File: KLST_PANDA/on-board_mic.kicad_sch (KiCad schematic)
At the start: 0 parts

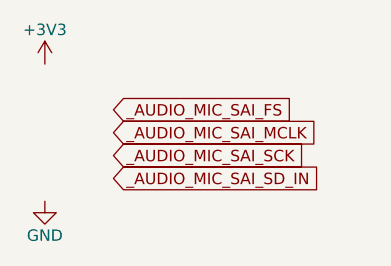
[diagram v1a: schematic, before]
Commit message: added PDM interface ( and removed SAI )
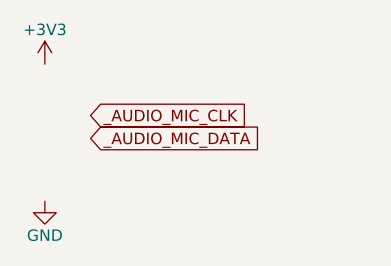
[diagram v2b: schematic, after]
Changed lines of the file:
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@@
 (kicad_sch (version 20230121) (generator eeschema)
   (paper "A4")
-  (global_label "_AUDIO_MIC_SAI_MCLK" (shape input) (at 142.875 101.6 0) (fields_autoplaced)
+  (global_label "_AUDIO_MIC_CLK" (shape input) (at 140.335 99.695 0) (fields_autoplaced)
     (effects (font (size 1.27 1.27)) (justify left))
-    (property "Intersheetrefs" "${INTERSHEET_REFS}" (at 166.5242 101.6 0)
+    (property "Intersheetrefs" "${INTERSHEET_REFS}" (at 158.6623 99.695 0)
       (effects (font (size 1.27 1.27)) (justify left) hide)
     )
   )
-  (global_label "_AUDIO_MIC_SAI_SD_IN" (shape input) (at 142.875 106.68 0) (fields_autoplaced)
+  (global_label "_AUDIO_MIC_DATA" (shape input) (at 140.335 102.235 0) (fields_autoplaced)
     (effects (font (size 1.27 1.27)) (justify left))
-    (property "Intersheetrefs" "${INTERSHEET_REFS}" (at 166.8871 106.68 0)
+    (property "Intersheetrefs" "${INTERSHEET_REFS}" (at 159.509 102.235 0)
       (effects (font (size 1.27 1.27)) (justify left) hide)
     )
-  )
-  (global_label "_AUDIO_MIC_SAI_FS" (shape input) (at 142.875 99.06 0) (fields_autoplaced)
-    (effects (font (size 1.27 1.27)) (justify left))
-    (property "Intersheetrefs" "${INTERSHEET_REFS}" (at 163.8028 99.06 0)
-      (effects (font (size 1.27 1.27)) (justify left) hide)
-    )
-  )
-  (global_label "_AUDIO_MIC_SAI_SCK" (shape input) (at 142.875 104.14 0) (fields_autoplaced)
-    (effects (font (size 1.27 1.27)) (justify left))
-    (property "Intersheetrefs" "${INTERSHEET_REFS}" (at 165.2542 104.14 0)
-      (effects (font (size 1.27 1.27)) (justify left) hide)
-    )

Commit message: added MEMS mics
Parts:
- added C72: 100nF, symbol Device:C_Small
- added C73: 1uF, symbol Device:C_Polarized_Small
- added U7, U8: MP34DT05TR-A, MP34DT05TR-A_STM, symbol MP34DT05TR-A:MP34DT05TR-A
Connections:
- net +3V3: now also C72.1, C73.1, U7.1 (VDD), U7.2 (LR), U8.1 (VDD)
- net GND: now also C72.2, C73.2, U7.5 (GND), U8.2 (LR), U8.5 (GND)
- net _AUDIO_MIC_CLK: now also U7.3 (CLK), U8.3 (CLK)
- net _AUDIO_MIC_DATA: now also U7.4 (DOUT), U8.4 (DOUT)
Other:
- note added: "on-board microphones"

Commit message: added mechanical keys, updated audio jacks, minor changes
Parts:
- U7, U8: footprint MP34DT05TR-A_STM -> MP34DT05TR-A:MP34DT05TR-A_STM
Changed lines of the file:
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@@
       (effects (font (size 1.524 1.524)))
     )
-    (property "Footprint" "MP34DT05TR-A_STM" (at 110.49 93.98 0)
+    (property "Footprint" "MP34DT05TR-A:MP34DT05TR-A_STM" (at 110.49 93.98 0)
       (effects (font (size 1.27 1.27) italic) hide)
     )
@@
       (effects (font (size 1.524 1.524)))
     )
-    (property "Footprint" "MP34DT05TR-A_STM" (at 110.49 118.745 0)
+    (property "Footprint" "MP34DT05TR-A:MP34DT05TR-A_STM" (at 110.49 118.745 0)
       (effects (font (size 1.27 1.27) italic) hide)
     )

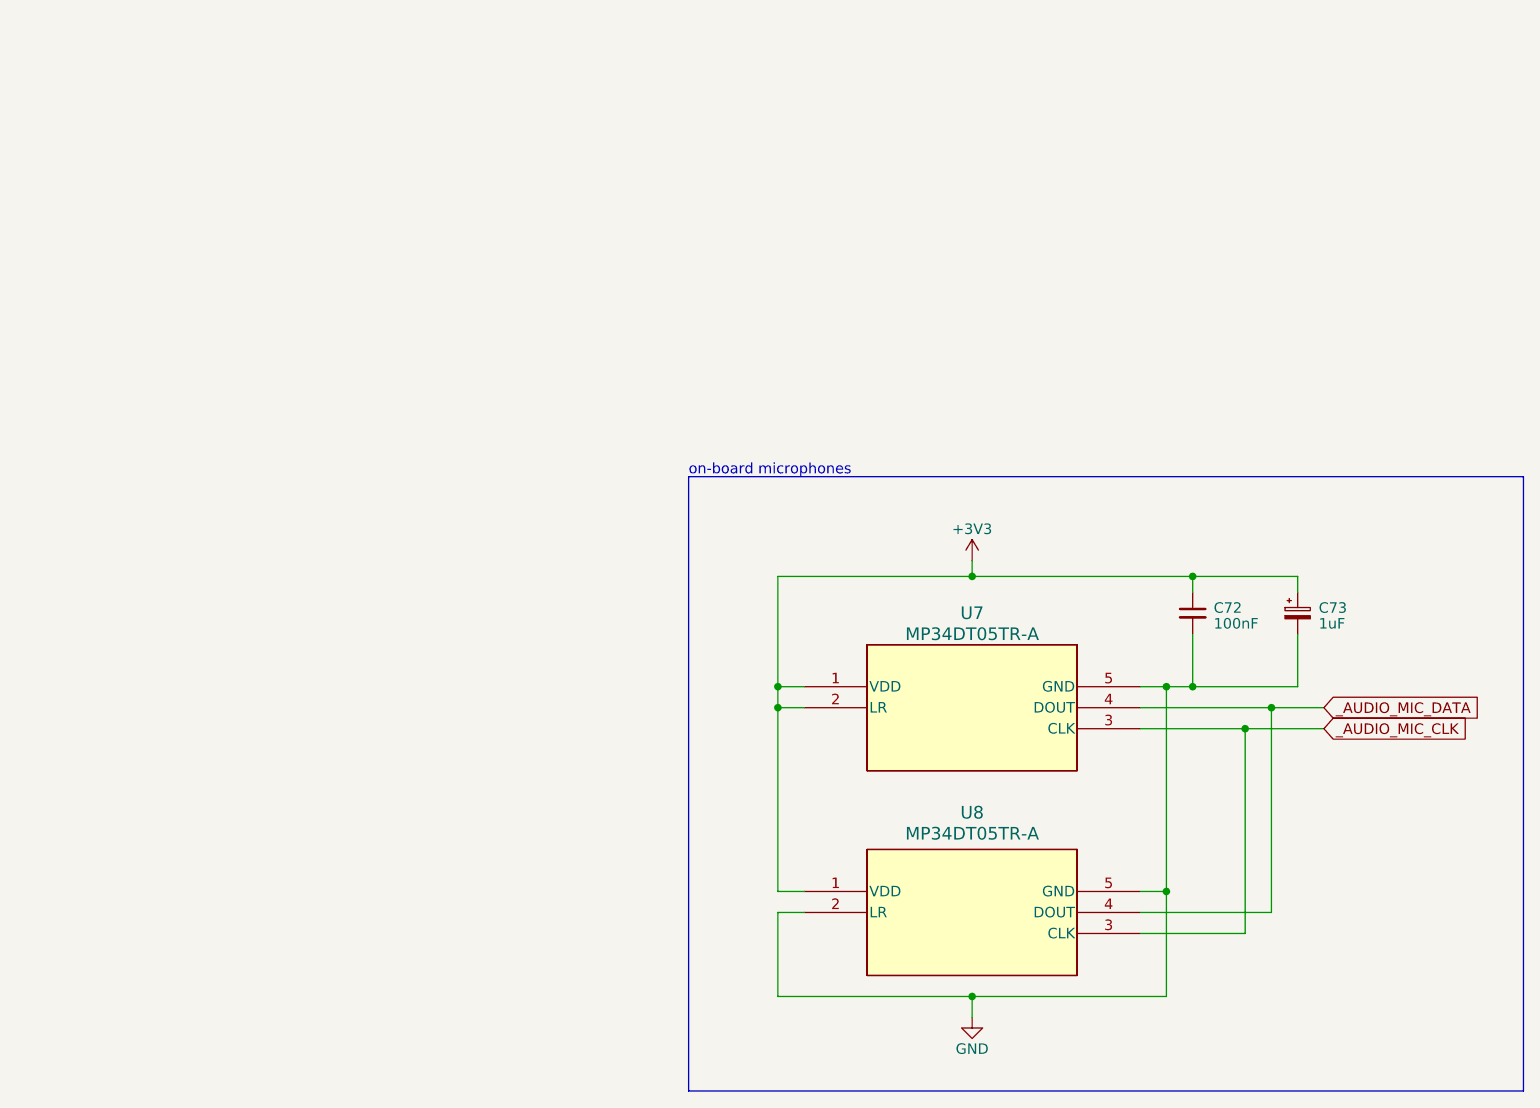
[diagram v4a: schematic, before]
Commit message: moved core (MCU) to sheet, cleaned up sheets
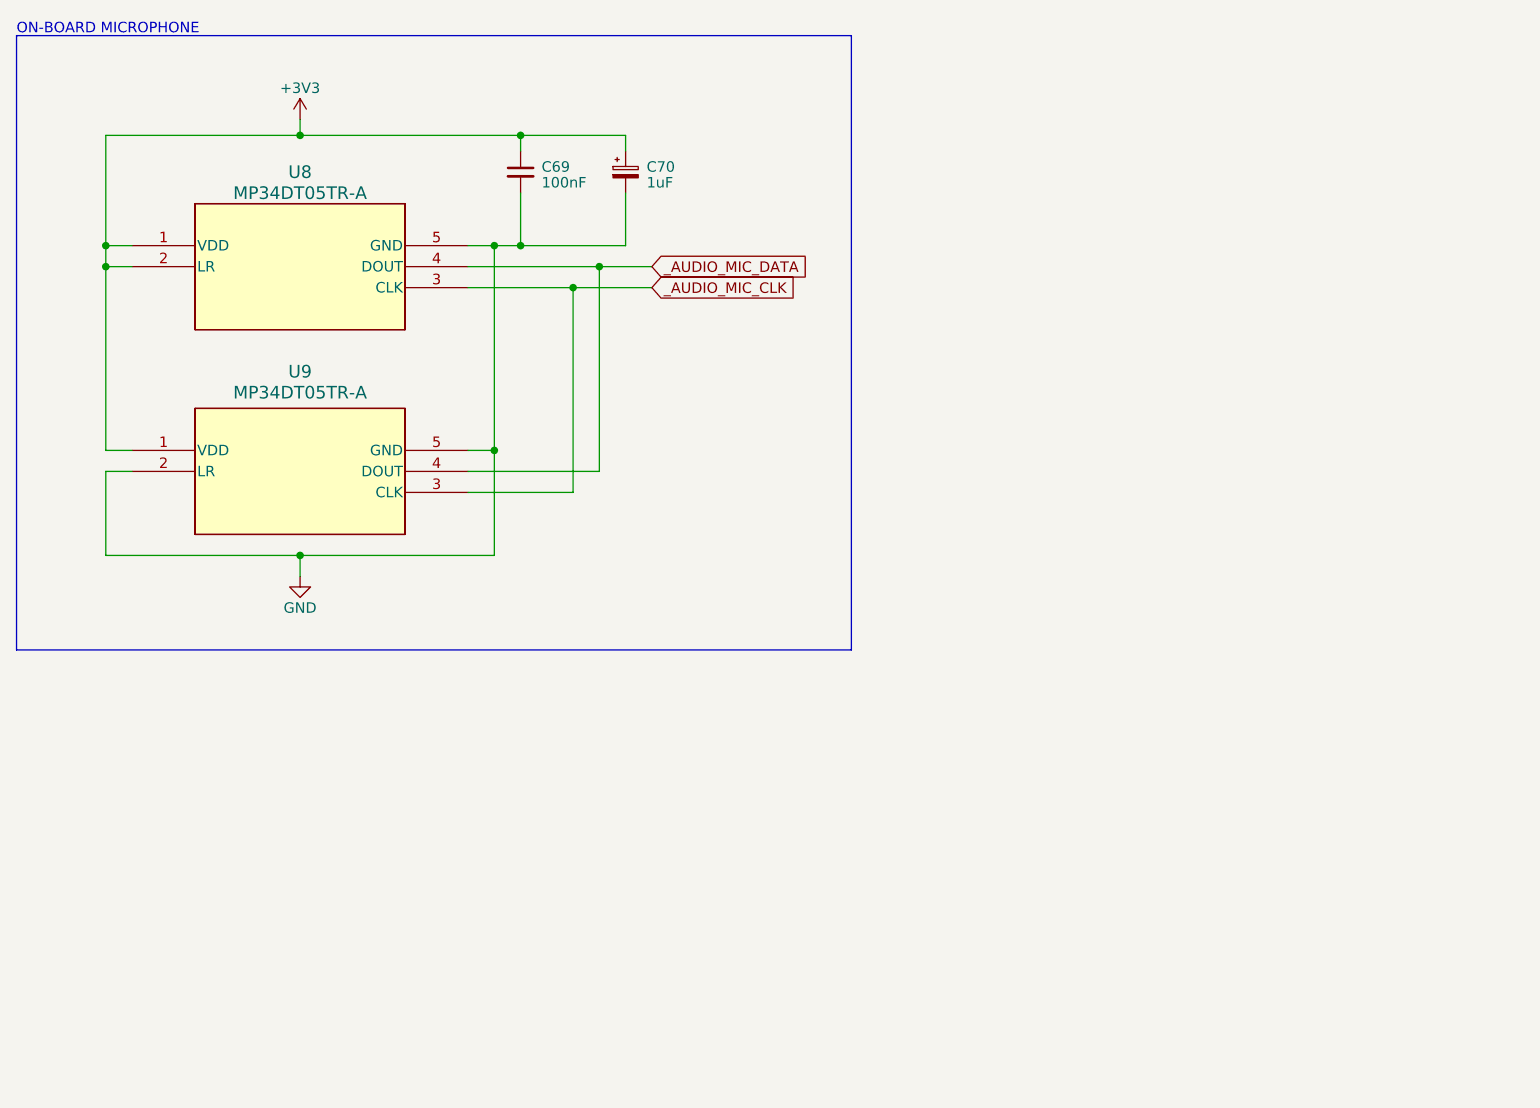
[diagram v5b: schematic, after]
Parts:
- renumbered C72 to C69, C73 to C70, U7 to U8, U8 to U9
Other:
- note added: "ON-BOARD MICROPHONE"
- note removed: "on-board microphones"
- moved on the sheet: C69, C70, U8, U9

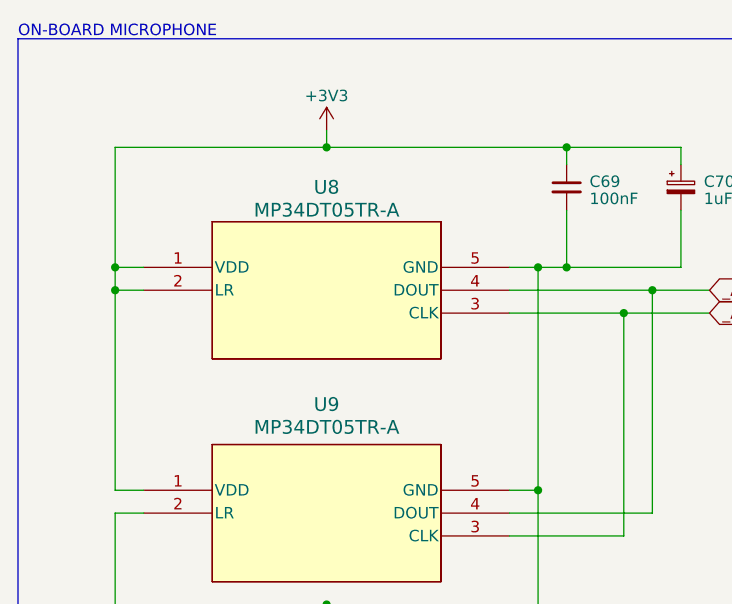
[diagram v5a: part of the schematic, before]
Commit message: started cleaning up schematic ( addressing DRC errors/warning ) (WIP)
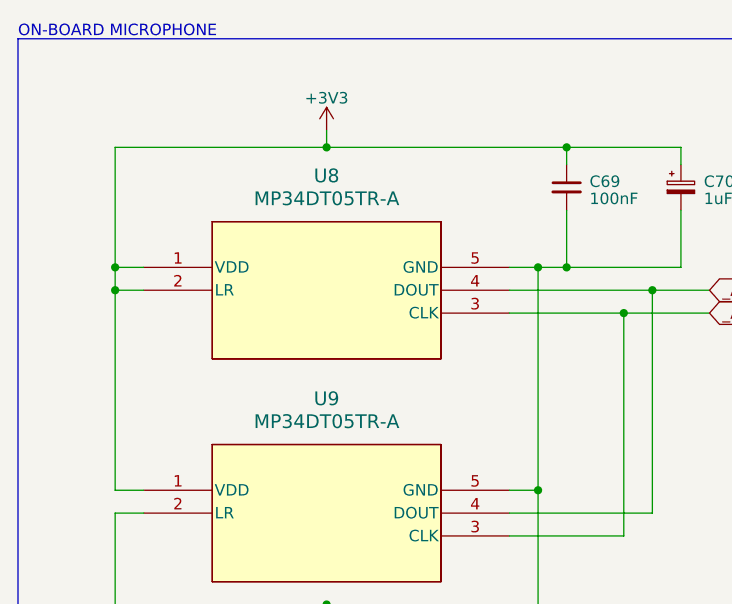
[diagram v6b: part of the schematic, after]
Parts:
- U8, U9: footprint MP34DT05TR-A:MP34DT05TR-A_STM -> MP34DT05TR-A_STM
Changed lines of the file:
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@@
       (effects (font (size 1.27 1.27)) hide)
     )
-    (property "Value" "+3V3" (at 49.53 21.59 0)
+    (property "Value" "+3V3" (at 49.53 21.844 0)
       (effects (font (size 1.27 1.27)))
     )
@@
         )
         (path "/b4513875-4c57-4720-bcc5-43ead67fe18f/47e8e77e-c64e-4c44-bfd8-2073580a3d85"
-          (reference "#PWR088") (unit 1)
+          (reference "#PWR089") (unit 1)
         )
       )
@@
   (symbol (lib_name "MP34DT05TR-A_1") (lib_id "MP34DT05TR-A:MP34DT05TR-A") (at 29.21 40.64 0) (unit 1)
     (in_bom yes) (on_board yes) (dnp no) (fields_autoplaced)
-    (property "Reference" "U8" (at 49.53 31.75 0)
+    (property "Reference" "U8" (at 49.53 30.48 0)
       (effects (font (size 1.524 1.524)))
     )
-    (property "Value" "MP34DT05TR-A" (at 49.53 34.29 0)
+    (property "Value" "MP34DT05TR-A" (at 49.53 33.02 0)
       (effects (font (size 1.524 1.524)))
     )
-    (property "Footprint" "MP34DT05TR-A:MP34DT05TR-A_STM" (at 29.21 40.64 0)
+    (property "Footprint" "MP34DT05TR-A_STM" (at 29.21 40.64 0)
       (effects (font (size 1.27 1.27) italic) hide)
     )
@@
     )
     (pin "1")
-    (pin "2")
     (pin "3")
     (pin "4")
+    (pin "2")
     (pin "5")
     (instances
@@
         )
         (path "/b4513875-4c57-4720-bcc5-43ead67fe18f/47e8e77e-c64e-4c44-bfd8-2073580a3d85"
-          (reference "#PWR089") (unit 1)
+          (reference "#PWR090") (unit 1)
         )
       )
@@
   (symbol (lib_id "MP34DT05TR-A:MP34DT05TR-A") (at 29.21 65.405 0) (unit 1)
     (in_bom yes) (on_board yes) (dnp no) (fields_autoplaced)
-    (property "Reference" "U9" (at 49.53 55.88 0)
+    (property "Reference" "U9" (at 49.53 55.245 0)
       (effects (font (size 1.524 1.524)))
     )
-    (property "Value" "MP34DT05TR-A" (at 49.53 58.42 0)
+    (property "Value" "MP34DT05TR-A" (at 49.53 57.785 0)
       (effects (font (size 1.524 1.524)))
     )
-    (property "Footprint" "MP34DT05TR-A:MP34DT05TR-A_STM" (at 29.21 65.405 0)
+    (property "Footprint" "MP34DT05TR-A_STM" (at 29.21 65.405 0)
       (effects (font (size 1.27 1.27) italic) hide)
     )
@@
     )
     (pin "1")
-    (pin "2")
     (pin "3")
     (pin "4")
+    (pin "2")
     (pin "5")
     (instances

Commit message: added battery clip, updated to new KiCad version
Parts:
- U8, U9: footprint MP34DT05TR-A_STM -> MP34DT05TR-A:MP34DT05TR-A_STM
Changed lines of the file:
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@@
       (effects (font (size 1.524 1.524)))
     )
-    (property "Footprint" "MP34DT05TR-A_STM" (at 29.21 40.64 0)
+    (property "Footprint" "MP34DT05TR-A:MP34DT05TR-A_STM" (at 29.21 40.64 0)
       (effects (font (size 1.27 1.27) italic) hide)
     )
@@
       (effects (font (size 1.524 1.524)))
     )
-    (property "Footprint" "MP34DT05TR-A_STM" (at 29.21 65.405 0)
+    (property "Footprint" "MP34DT05TR-A:MP34DT05TR-A_STM" (at 29.21 65.405 0)
       (effects (font (size 1.27 1.27) italic) hide)
     )

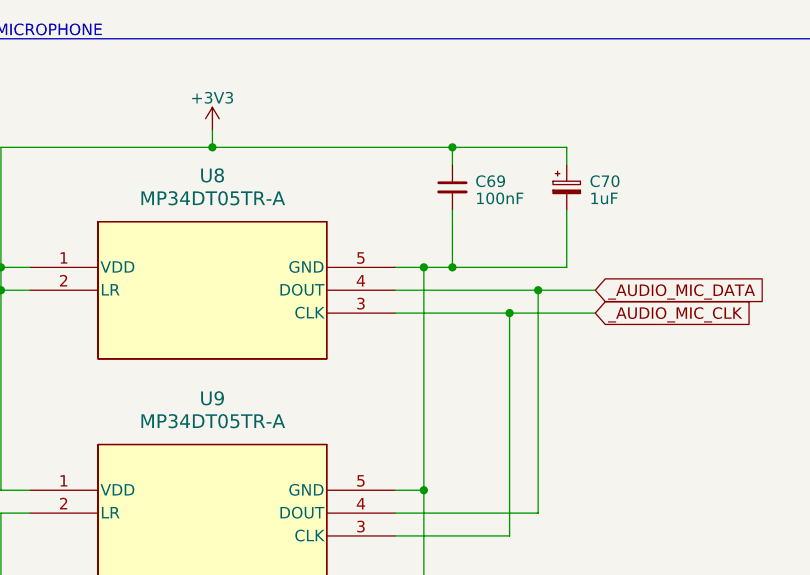
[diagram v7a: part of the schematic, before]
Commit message: removed DRC warnings and error, added power page
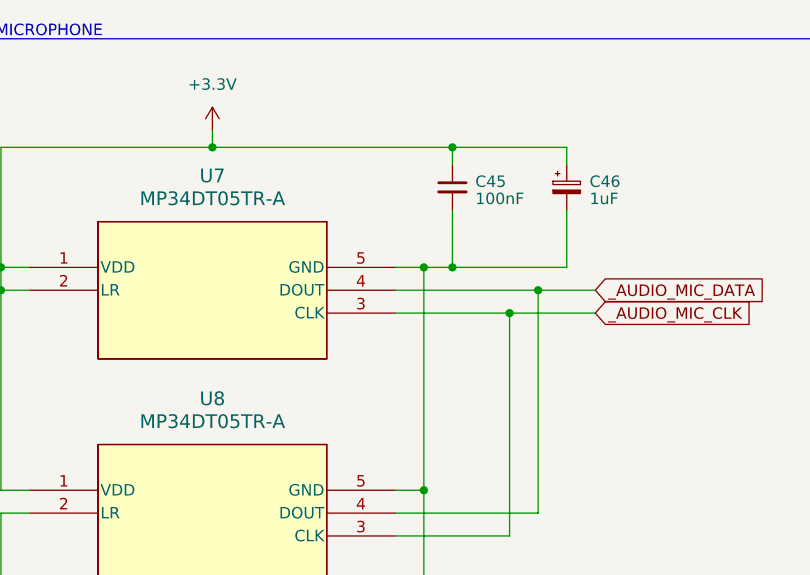
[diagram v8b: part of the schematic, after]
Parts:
- renumbered C69 to C45, C70 to C46, U8 to U7, U9 to U8
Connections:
- net +3V3 renamed +3.3V
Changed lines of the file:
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@@
+    )
+  )
+  (symbol (lib_id "power:+3.3V") (at 49.53 25.4 0) (unit 1)
+    (in_bom yes) (on_board yes) (dnp no) (fields_autoplaced)
+    (property "Reference" "#PWR080" (at 49.53 29.21 0)
+      (effects (font (size 1.27 1.27)) hide)
+    )
+    (property "Value" "+3.3V" (at 49.53 20.32 0)
+      (effects (font (size 1.27 1.27)))
+    )
+    (property "Footprint" "" (at 49.53 25.4 0)
+      (effects (font (size 1.27 1.27)) hide)
+    )
+    (property "Datasheet" "" (at 49.53 25.4 0)
+      (effects (font (size 1.27 1.27)) hide)
+    )
+    (pin "1")
+    (instances
+      (project "KLST_PANDA"
+        (path "/b4513875-4c57-4720-bcc5-43ead67fe18f/47e8e77e-c64e-4c44-bfd8-2073580a3d85"
+          (reference "#PWR080") (unit 1)
+        )
+      )
     )
   )
   (symbol (lib_id "Device:C_Polarized_Small") (at 88.9 31.75 0) (unit 1)
     (in_bom yes) (on_board yes) (dnp no)
-    (property "Reference" "C70" (at 91.44 31.115 0)
+    (property "Reference" "C46" (at 91.44 31.115 0)
       (effects (font (size 1.27 1.27)) (justify left))
     )
@@
       (project "KLST_PANDA"
         (path "/b4513875-4c57-4720-bcc5-43ead67fe18f/47e8e77e-c64e-4c44-bfd8-2073580a3d85"
-          (reference "C70") (unit 1)
+          (reference "C46") (unit 1)
         )
       )
     )
   )
-  (symbol (lib_id "power:+3V3") (at 49.53 25.4 0) (unit 1)
-    (in_bom yes) (on_board yes) (dnp no)
-    (property "Reference" "#PWR0127" (at 49.53 29.21 0)
-      (effects (font (size 1.27 1.27)) hide)
-    )
-    (property "Value" "+3V3" (at 49.53 21.844 0)
-      (effects (font (size 1.27 1.27)))
-    )
-    (property "Footprint" "" (at 49.53 25.4 0)
-      (effects (font (size 1.27 1.27)) hide)
-    )
-    (property "Datasheet" "" (at 49.53 25.4 0)
-      (effects (font (size 1.27 1.27)) hide)
-    )
-    (pin "1")
-    (instances
-      (project "KLST_PANDA"
-        (path "/b4513875-4c57-4720-bcc5-43ead67fe18f"
-          (reference "#PWR0127") (unit 1)
-        )
-        (path "/b4513875-4c57-4720-bcc5-43ead67fe18f/47e8e77e-c64e-4c44-bfd8-2073580a3d85"
-          (reference "#PWR089") (unit 1)
-        )
-      )
-    )
-  )
-  (symbol (lib_name "MP34DT05TR-A_1") (lib_id "MP34DT05TR-A:MP34DT05TR-A") (at 29.21 40.64 0) (unit 1)
+  (symbol (lib_id "MP34DT05TR-A:MP34DT05TR-A") (at 29.21 40.64 0) (unit 1)
     (in_bom yes) (on_board yes) (dnp no) (fields_autoplaced)
-    (property "Reference" "U8" (at 49.53 30.48 0)
+    (property "Reference" "U7" (at 49.53 30.48 0)
       (effects (font (size 1.524 1.524)))
     )
@@
       (project "KLST_PANDA"
         (path "/b4513875-4c57-4720-bcc5-43ead67fe18f/47e8e77e-c64e-4c44-bfd8-2073580a3d85"
-          (reference "U8") (unit 1)
+          (reference "U7") (unit 1)
         )
       )
@@
   (symbol (lib_id "Device:C_Small") (at 76.2 31.75 0) (unit 1)
     (in_bom yes) (on_board yes) (dnp no)
-    (property "Reference" "C69" (at 78.74 31.115 0)
+    (property "Reference" "C45" (at 78.74 31.115 0)
       (effects (font (size 1.27 1.27)) (justify left))
     )
@@
       (project "KLST_PANDA"
         (path "/b4513875-4c57-4720-bcc5-43ead67fe18f/47e8e77e-c64e-4c44-bfd8-2073580a3d85"
-          (reference "C69") (unit 1)
+          (reference "C45") (unit 1)
         )
       )
@@
         )
         (path "/b4513875-4c57-4720-bcc5-43ead67fe18f/47e8e77e-c64e-4c44-bfd8-2073580a3d85"
-          (reference "#PWR090") (unit 1)
+          (reference "#PWR081") (unit 1)
         )
       )
@@
   (symbol (lib_id "MP34DT05TR-A:MP34DT05TR-A") (at 29.21 65.405 0) (unit 1)
     (in_bom yes) (on_board yes) (dnp no) (fields_autoplaced)
-    (property "Reference" "U9" (at 49.53 55.245 0)
+    (property "Reference" "U8" (at 49.53 55.245 0)
       (effects (font (size 1.524 1.524)))
     )
@@
       (project "KLST_PANDA"
         (path "/b4513875-4c57-4720-bcc5-43ead67fe18f/47e8e77e-c64e-4c44-bfd8-2073580a3d85"
-          (reference "U9") (unit 1)
+          (reference "U8") (unit 1)
         )
       )
